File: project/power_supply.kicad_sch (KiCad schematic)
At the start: 20 parts, among them J1 USB_C_Receptacle_USB2.0_16P, U1 LD1117S33CTR, U2 LD1117S12CTR, U3 USBLC6-2SC6

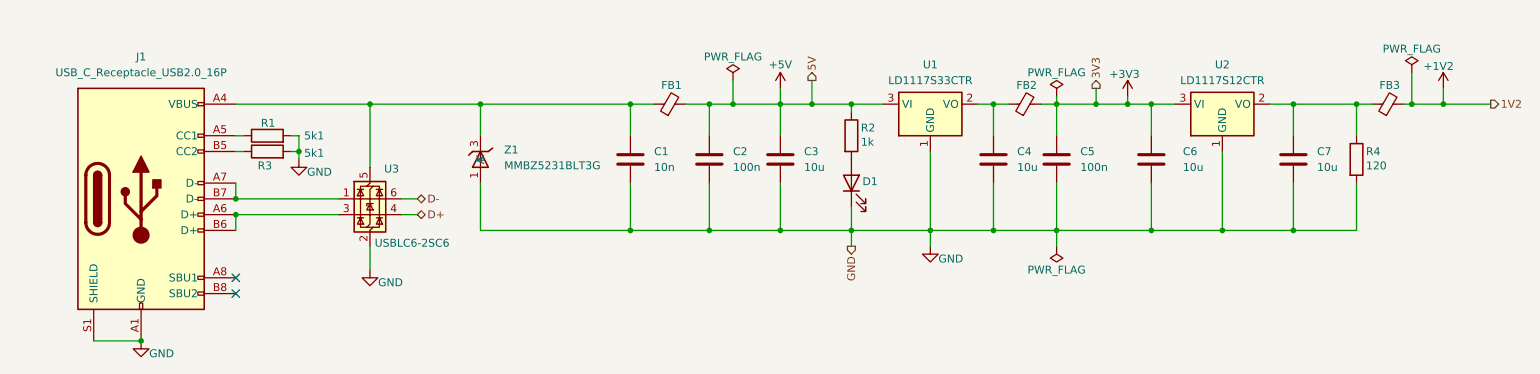
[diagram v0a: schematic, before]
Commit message: cambios en disposicion de esquematico
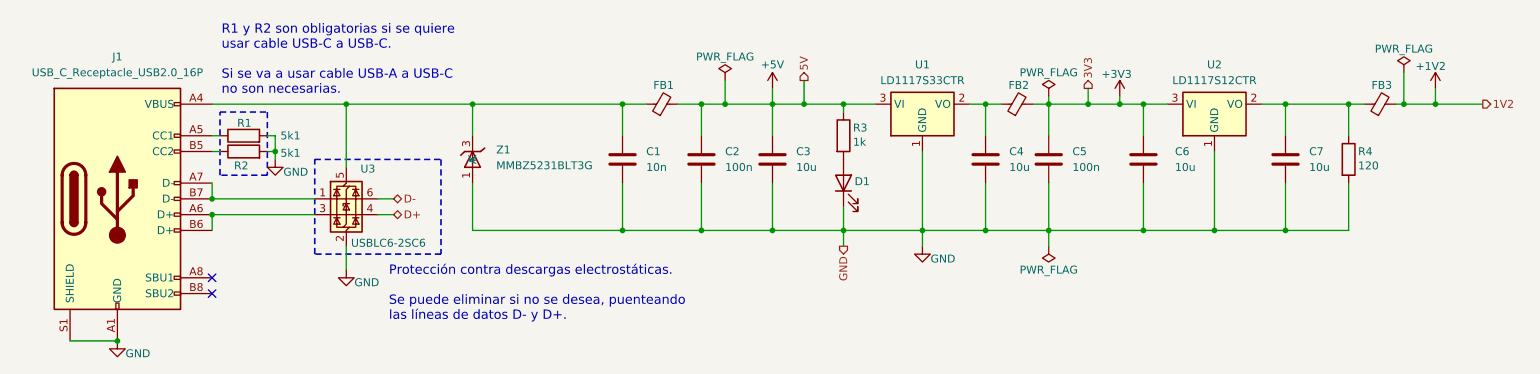
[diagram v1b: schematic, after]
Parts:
- renumbered R3 to R2, R2 to R3
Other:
- note added: "Protección contra descargas electrostáticas. Se puede eliminar si no se desea, puenteando las líneas de datos D- y D+."
- note added: "R1 y R2 son obligatorias si se quiere usar cable USB-C a USB-C. Si se va a usar cable USB-A a USB-C no son necesarias."
- moved on the sheet: C1, C2, C3, C4, C5, C6, C7, D1, FB1, FB2, FB3, J1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

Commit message: Corregidos footprints, generada nuevas capturas, cambiado regulador por TLV761
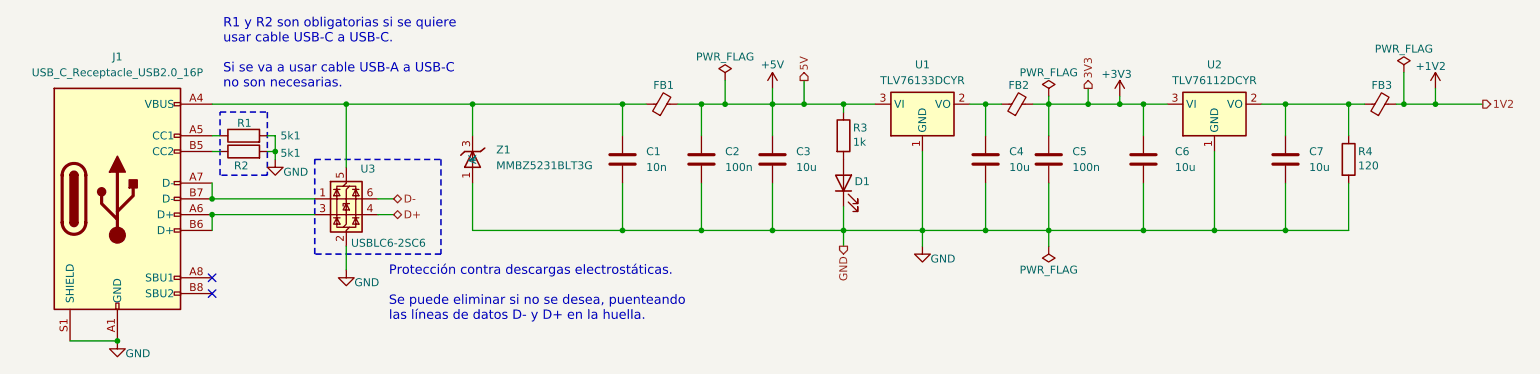
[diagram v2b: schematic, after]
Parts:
- removed U1: LD1117S33CTR, Package_TO_SOT_SMD:SOT-223-3_TabPin2, symbol Regulator_Linear:LD1117S33TR_SOT223
- removed U2: LD1117S12CTR, Package_TO_SOT_SMD:SOT-223-3_TabPin2, symbol Regulator_Linear:LD1117S12TR_SOT223
- added U1: TLV76133DCYR, Package_TO_SOT_SMD:SOT-223-3_TabPin2, symbol Regulator_Linear:TLV76133DCY
- added U2: TLV76112DCYR, Package_TO_SOT_SMD:SOT-223-3_TabPin2, symbol Regulator_Linear:TLV76133DCY
- FB1, FB2, FB3: footprint Inductor_SMD:L_1206_3216Metric_Pad1.42x1.75mm_HandSolder -> Inductor_SMD:L_1206_3216Metric
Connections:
- net +3V3: now also U2.3 (VI)
- net +5V: now also U1.3 (VI)
- net GND: now also U1.1 (GND), U2.1 (GND)
- net at C7.1, FB3.1, R4.1: now also U2.2 (VO)
- net at C4.1, FB2.1: now also U1.2 (VO)
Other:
- note added: "Protección contra descargas electrostáticas. Se puede eliminar si no se desea, puenteando las líneas de datos D- y D+ en la huella."
- note removed: "Protección contra descargas electrostáticas. Se puede eliminar si no se desea, puenteando las líneas de datos D- y D+."

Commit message: Agregado datasheet faltante y completado cuadro de BOM con sus links
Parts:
- U1: Código del fabricante (Order Code) (none) -> TLV76133DCYR; Código del vendedor (Provider Order Code) (none) -> 595-TLV76133DCYR; Fabricante (none) -> Texas Instruments; Package (none) -> SOT-223-4
- U2: Código del fabricante (Order Code) (none) -> TLV76112DCYR; Código del vendedor (Provider Order Code) (none) -> 595-TLV76112DCYR; Fabricante (none) -> Texas Instruments; Package (none) -> SOT-223-4
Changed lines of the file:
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@@
+			)
+		)
+		(property "Código del fabricante (Order Code)" "TLV76133DCYR "
+			(at 175.26 76.2 0)
+			(hide yes)
+			(show_name no)
+			(do_not_autoplace no)
+			(effects
+				(font
+					(size 1.27 1.27)
+				)
+			)
+		)
+		(property "Código del vendedor (Provider Order Code)" " 595-TLV76133DCYR"
+			(at 175.26 76.2 0)
+			(hide yes)
+			(show_name no)
+			(do_not_autoplace no)
+			(effects
+				(font
+					(size 1.27 1.27)
+				)
+			)
+		)
+		(property "Fabricante" "Texas Instruments"
+			(at 175.26 76.2 0)
+			(hide yes)
+			(show_name no)
+			(do_not_autoplace no)
+			(effects
+				(font
+					(size 1.27 1.27)
+				)
+			)
+		)
+		(property "Package" "SOT-223-4"
+			(at 175.26 76.2 0)
+			(hide yes)
+			(show_name no)
+			(do_not_autoplace no)
+			(effects
+				(font
+					(size 1.27 1.27)
+				)
 			)
 		)
@@
 			)
 		)
+		(property "Código del fabricante (Order Code)" "TLV76112DCYR "
+			(at 222.25 76.2 0)
+			(hide yes)
+			(show_name no)
+			(do_not_autoplace no)
+			(effects
+				(font
+					(size 1.27 1.27)
+				)
+			)
+		)
+		(property "Código del vendedor (Provider Order Code)" " 595-TLV76112DCYR"
+			(at 222.25 76.2 0)
+			(hide yes)
+			(show_name no)
+			(do_not_autoplace no)
+			(effects
+				(font
+					(size 1.27 1.27)
+				)
+			)
+		)
+		(property "Fabricante" "Texas Instruments"
+			(at 222.25 76.2 0)
+			(hide yes)
+			(show_name no)
+			(do_not_autoplace no)
+			(effects
+				(font
+					(size 1.27 1.27)
+				)
+			)
+		)
+		(property "Package" "SOT-223-4"
+			(at 222.25 76.2 0)
+			(hide yes)
+			(show_name no)
+			(do_not_autoplace no)
+			(effects
+				(font
+					(size 1.27 1.27)
+				)
+			)
+		)
 		(pin "3"
 		)
@@
 			)
 		)
-		(property "Datasheet" ""
+		(property "Datasheet" "https://www.we-online.com/components/products/datasheet/150141RS73100.pdf"
 			(at 162.56 88.9 0)
 			(hide yes)
